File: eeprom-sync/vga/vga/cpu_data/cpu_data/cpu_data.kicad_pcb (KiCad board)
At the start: 2 copper layers, 91.4 x 44.5 mm, 26 parts, among them J1 Conn_01x06_Female, J10 Conn_01x03_Female, J11 Conn_01x02_Female, J2 Conn_01x02_Female, J3 Conn_01x04_Female, J4 Conn_01x15_Female, J5 Conn_01x15_Female, J6 Conn_01x08_Female, J7 Conn_01x02_Female, J8 Conn_01x02_Female, J9 Conn_01x08_Female, U1 GAL22V10, U2 SN74ACT08, U3 74HC273

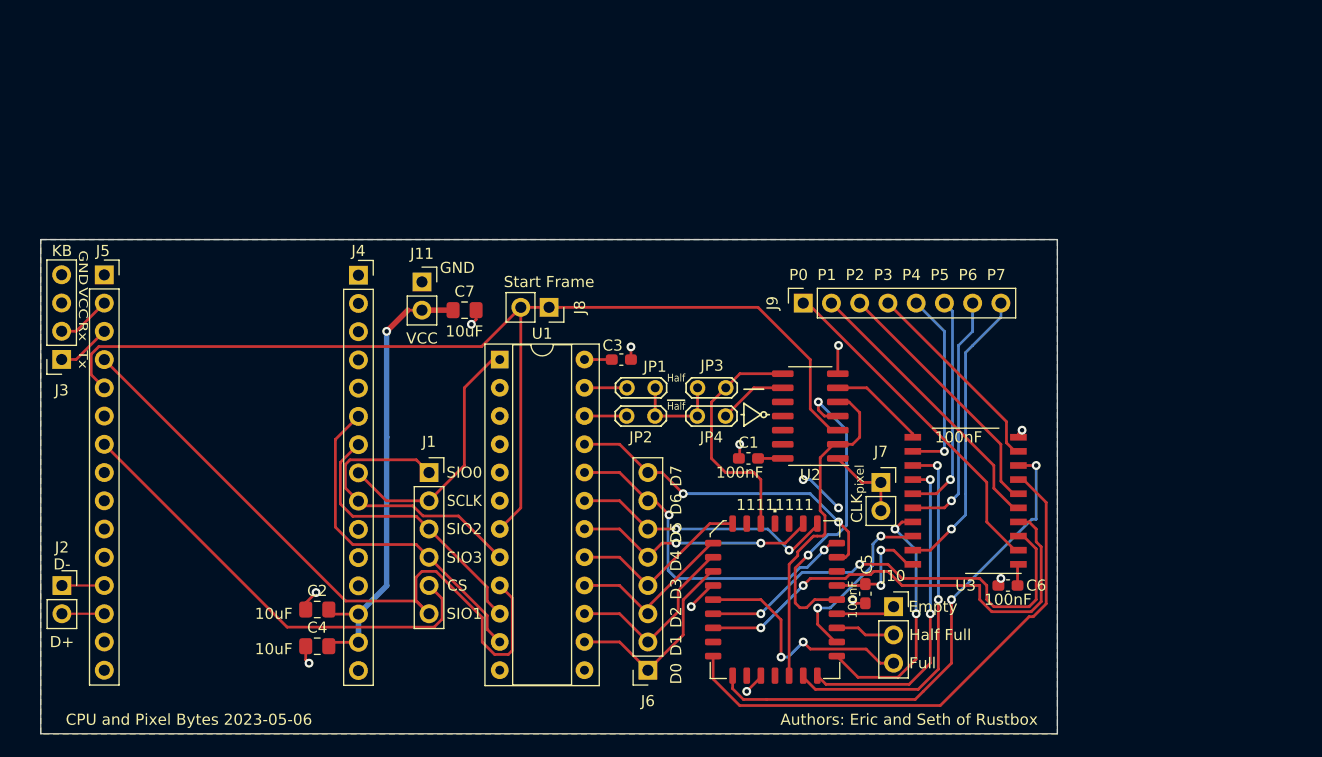
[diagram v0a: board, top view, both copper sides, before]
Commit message: cpu data now uses RC circuits for timing instead of not gates
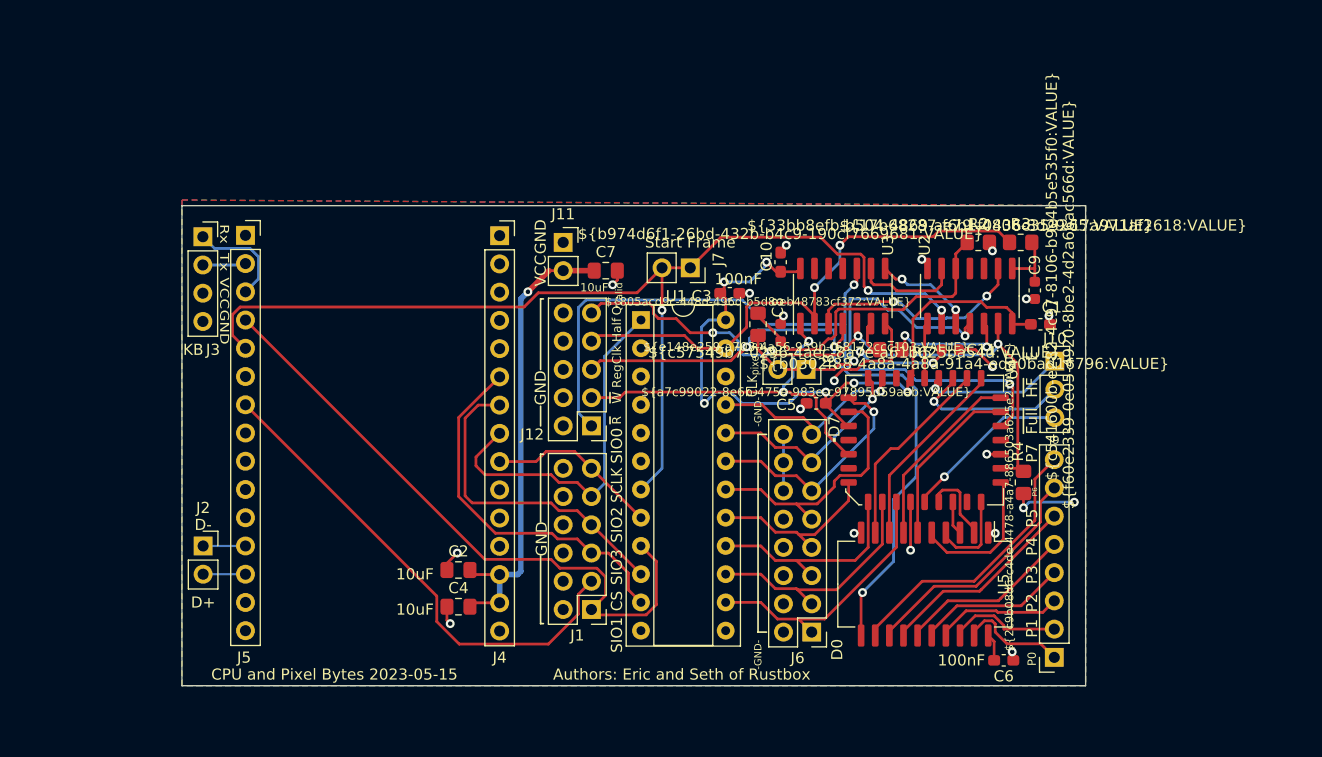
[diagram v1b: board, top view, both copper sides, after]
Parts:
- removed 11111111: IDT7205L12JG, Package_LCC:PLCC-32_11.4x14.0mm_P1.27mm
- removed JP1, JP2, JP3, JP4: Jumper_2_Open, TestPoint:TestPoint_2Pads_Pitch2.54mm_Drill0.8mm
- added C10: 100nF, Capacitor_SMD:C_0603_1608Metric_Pad1.08x0.95mm_HandSolder, F.Cu at (130.0, 65.5)
- added C11: 100pF, Capacitor_SMD:C_0603_1608Metric, F.Cu at (145.3, 73.4)
- added C8: 6.2pF, Capacitor_SMD:C_0603_1608Metric, F.Cu at (130.0, 71.9)
- added C9: 100pF, Capacitor_SMD:C_0603_1608Metric, F.Cu at (152.9, 68.1)
- added J12: Conn_02x05_Odd_Even, Connector_PinHeader_2.54mm:PinHeader_2x05_P2.54mm_Vertical, F.Cu at (113.0, 80.3)
- added R1: 900, Resistor_SMD:R_0805_2012Metric_Pad1.20x1.40mm_HandSolder, F.Cu at (128.0, 71.1)
- added R2: 600, Resistor_SMD:R_0805_2012Metric_Pad1.20x1.40mm_HandSolder, F.Cu at (147.8, 63.8)
- added R3: 59, Resistor_SMD:R_0805_2012Metric_Pad1.20x1.40mm_HandSolder, F.Cu at (151.6, 63.8)
- added R4: 10k, Resistor_SMD:R_0805_2012Metric_Pad1.20x1.40mm_HandSolder, F.Cu at (151.9, 85.3)
- added R5: 66.5, Resistor_SMD:R_0805_2012Metric_Pad1.20x1.40mm_HandSolder, F.Cu at (140.0, 73.4)
- added U4: IDT7205L12JG, Package_LCC:PLCC-32_11.4x14.0mm_P1.27mm, F.Cu at (143.0, 81.5)
- added U5: 74LS573, Package_SO:SOIC-20W_7.5x15.4mm_P1.27mm, F.Cu at (143.0, 94.5)
- J1: value Conn_01x06_Female -> Conn_02x06_Odd_Even; footprint Connector_PinSocket_2.54mm:PinSocket_1x06_P2.54mm_Vertical -> Connector_PinHeader_2.54mm:PinHeader_2x06_P2.54mm_Vertical
- J6: value Conn_01x08_Female -> Conn_02x08_Odd_Even; footprint Connector_PinSocket_2.54mm:PinSocket_1x08_P2.54mm_Vertical -> Connector_PinHeader_2.54mm:PinHeader_2x08_P2.54mm_Vertical
- U2: value SN74ACT08 -> 74HC14
- U3: value 74HC273 -> 74LS02; footprint Package_SO:SO-20_12.8x7.5mm_P1.27mm -> Package_SO:SOIC-14_3.9x8.7mm_P1.27mm
- moved J9 39.1 mm to (154.7, 101.1), turned to 180 degrees
- moved C1 28.9 mm to (153.4, 71.1), turned to 180 degrees
- moved J10 26.4 mm to (154.7, 74.4)
- moved J7 25.8 mm to (121.9, 66.0), turned to -90 degrees
- moved J8 23.8 mm to (132.3, 75.2)
- moved U3 21.5 mm to (135.6, 68.6), turned to 90 degrees
- moved J1 19.1 mm to (113.0, 96.8), turned to 180 degrees
- moved U2 18.0 mm to (147.1, 68.6), turned to -90 degrees
- moved C5 17.7 mm to (133.2, 78.2), turned to 0 degrees
- moved J3 16.8 mm to (78.1, 63.2), turned to 0 degrees
- moved J6 15.1 mm to (132.8, 98.8)
- moved U1 13.2 mm to (117.5, 70.7)
- moved C7 13.2 mm to (114.3, 66.3)
- moved J2 13.2 mm to (78.1, 91.1)
- moved J4 13.2 mm to (104.8, 63.1)
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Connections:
- J1 pad 1: /SIO0 -> /SIO1
- J1 pad 2: /SCLK -> GND
- J1 pad 3: /SIO2 -> /CS
- J1 pad 4: /SIO3 -> GND
- J1 pad 5: /CS -> /SIO3
- J1 pad 6: /SIO1 -> GND
- J3 pad 1: /KB_{Tx} -> /KB_{Rx}
- J3 pad 2: /KB_{Rx} -> /KB_{Tx}
- J5 pad 2: /KB_{Rx} -> /KB_{Tx}
- J5 pad 3: /KB_{Tx} -> /KB_{Rx}
- J6 pad 2: /D1 -> GND
- J6 pad 3: /D2 -> /D1
- J6 pad 4: /D3 -> GND
- J6 pad 5: /D4 -> /D2
- J6 pad 6: /D5 -> GND
- J6 pad 7: /D6 -> /D3
- J6 pad 8: /D7 -> GND
- J7 pad 1: /CLK_{pixel} -> /StartFrame
- J7 pad 2: /CLK_{pixel} -> /StartFrame
- J8 pad 1: /StartFrame -> /CLK_{pixel}
- J8 pad 2: /StartFrame -> /CLK_{pixel}
- U1 pad 22: Net-(JP2-Pad1) -> unconnected-(U1-Pad22)
- U1 pad 23: Net-(JP1-Pad1) -> /Half
- U2 pad 1: /CLK_{pixel} -> Net-(C9-Pad1)
- U2 pad 10: (no net) -> Net-(U2-Pad10)
- U2 pad 11: (no net) -> /CLK_{pixel}
- U2 pad 12: (no net) -> Net-(R5-Pad2)
- U2 pad 13: (no net) -> /Q_{valid}
- U2 pad 2: /~{R} -> Net-(U2-Pad2)
- U2 pad 3: /StartFrame -> (no net)
- U2 pad 4: /Reset -> (no net)
- U2 pad 5: /~{R} -> Net-(C8-Pad1)
- U2 pad 8: /~{W} -> /Reset
- U2 pad 9: Net-(JP4-Pad2) -> /StartFrame
- U3 pad 1: VCC -> /~{W}
- U3 pad 10: GND -> /~{R}
- U3 pad 11: Net-(U2-Pad6) -> (no net)
- U3 pad 12: /P4 -> (no net)
- U3 pad 13: /Q4 -> (no net)
- U3 pad 14: /Q5 -> VCC
- U3 pad 2: /P0 -> /Half
- U3 pad 3: /Q0 -> Net-(U2-Pad2)
- U3 pad 4: /Q1 -> /RegClk
- U3 pad 5: /P1 -> /Q_{valid}
- U3 pad 6: /P2 -> Net-(C11-Pad1)
- U3 pad 7: /Q2 -> GND
- U3 pad 8: /Q3 -> Net-(U2-Pad10)
- U3 pad 9: /P3 -> Net-(U2-Pad6)
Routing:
- net /RegClk: track 0.00 -> 60.9 mm, vias 0 -> 3
- net /Q_{valid}: track 0.00 -> 59.0 mm, vias 0 -> 4
- net VCC: track 62.9 -> 116.4 mm, vias 5 -> 9
- net /Half: track 0.00 -> 48.2 mm, vias 0 -> 2
- net /Q2: track 49.3 -> 7.90 mm
- net /Q1: track 42.8 -> 3.03 mm, vias 2 -> 0
- net /~{R}: track 30.5 -> 65.3 mm, vias 0 -> 2
- net /Q0: track 40.0 -> 7.01 mm, vias 2 -> 0
- net /Q3: track 45.4 -> 13.1 mm, vias 2 -> 0
- net Net-(C8-Pad1): track 0.00 -> 28.0 mm
- net /Reset: track 28.5 -> 5.02 mm, vias 2 -> 0
- net /CLK_{pixel}: track 7.31 -> 29.7 mm, vias 0 -> 2
- net /P0: track 30.3 -> 9.79 mm
- net GND: track 17.7 -> 37.9 mm, vias 11 -> 18
- net Net-(U2-Pad2): track 0.00 -> 20.1 mm, vias 0 -> 2
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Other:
- board size 91.4 x 44.5 mm -> 81.3 x 43.2 mm
- board text added: "${17b68287-f6b1-4806-8d29-17a971af2618:VALUE}"
- board text added: "${2c9b08d6-c4de-4478-a4a7-886503a625e2:VALUE}"
- board text added: "${33bb8efb-b504-4869-ae79-f0436c353265:VALUE}"
- board text added: "${805acd9c-448d-496d-b5d8-eb48783cf372:VALUE}"
- board text added: "${a7c99022-8e6b-475e-983e-c97895d59aab:VALUE}"
- board text added: "${b0302f88-4a8a-4a8a-91a4-eda0bad16796:VALUE}"
- board text added: "${b974d6f1-26bd-432b-b4c9-190cf7669681:VALUE}"
- board text added: "${c541600b-e282-4c97-8106-b9e4b5e535f0:VALUE}"
- board text added: "${c57549b7-0296-4aec-8a7e-a61b625ba54d:VALUE}"
- board text added: "${e148e259-a703-4a56-959b-f68172ccc103:VALUE}"
- board text added: "${f60e2339-0e05-4920-8be2-4d2a66ac566d:VALUE}"
- board text added: "-GND-"
- board text added: "CPU and Pixel Bytes 2023-05-15"
- board text added: "Q_{valid}"
- board text added: "RegClk"
- board text added: "~{E}"
- board text added: "~{Full}"
- board text added: "~{HF}"
- board text added: "~{R}"
- board text added: "~{W}"
- board text removed: "CPU and Pixel Bytes 2023-05-06"
- board text removed: "D1"
- board text removed: "D2"
- board text removed: "D3"
- board text removed: "D4"
- board text removed: "D5"
- board text removed: "D6"
- board text removed: "Empty"
- board text removed: "Full"
- board text removed: "Half Full"
- board text removed: "~{Half}"

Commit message: cpu data board has transistor included
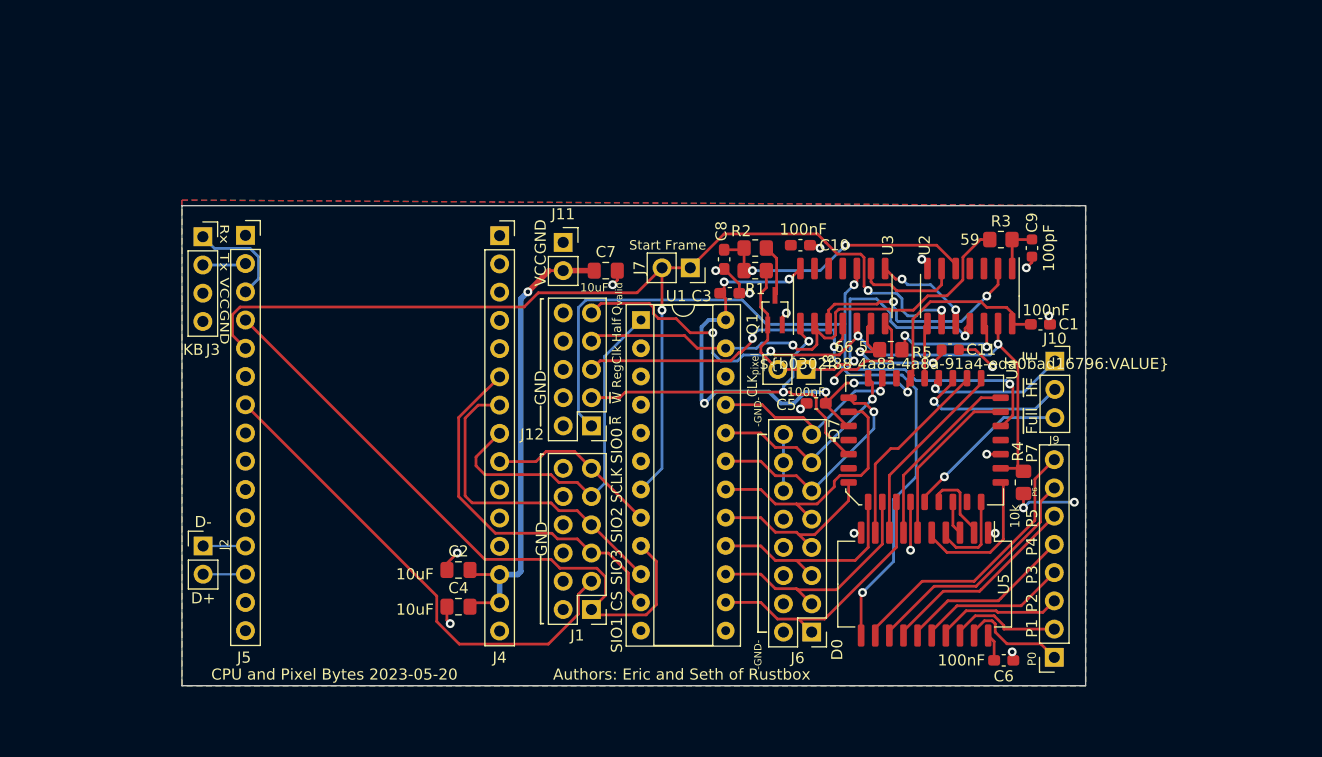
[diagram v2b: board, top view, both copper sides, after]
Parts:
- added Q1: Q_PNP_BEC, Package_TO_SOT_SMD:SOT-323_SC-70_Handsoldering, F.Cu at (129.5, 69.8)
- C8: value 6.2pF -> C_Small; footprint Capacitor_SMD:C_0603_1608Metric -> Capacitor_SMD:C_0603_1608Metric_Pad1.08x0.95mm_HandSolder
- J2: footprint Connector_PinSocket_2.54mm:PinSocket_1x02_P2.54mm_Vertical -> Connector_PinHeader_2.54mm:PinHeader_1x02_P2.54mm_Vertical
- R1: value 900 -> R
- R2: value 600 -> R
- moved R2 20.1 mm to (127.8, 64.3), turned to 180 degrees
- moved C8 8.32 mm to (125.0, 65.3), turned to -90 degrees
- moved R1 4.83 mm to (127.8, 66.3), turned to 180 degrees
- moved C9 3.82 mm to (152.7, 64.3)
- moved C10 2.34 mm to (131.8, 64.0), turned to 180 degrees
- moved R3 1.80 mm to (149.9, 63.5)
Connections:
- C8 pad 1: Net-(C8-Pad1) -> Net-(U2-Pad5)
- R1 pad 1: Net-(C8-Pad1) -> /CLK_{pixel}
- R1 pad 2: /CLK_{pixel} -> Net-(U2-Pad5)
- R2 pad 1: Net-(C8-Pad1) -> Net-(R2-Pad1)
- R2 pad 2: GND -> Net-(U2-Pad5)
- U2 pad 5: Net-(C8-Pad1) -> Net-(U2-Pad5)
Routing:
- net Net-(C8-Pad1): track 28.0 -> 0.00 mm
- net Net-(U2-Pad5): track 0.00 -> 25.0 mm, vias 0 -> 2
- net /CLK_{pixel}: track 29.7 -> 36.6 mm
- net Net-(R2-Pad1): track 0.00 -> 4.70 mm
- net GND: track 37.9 -> 41.6 mm
- net /Half: track 48.2 -> 46.2 mm, vias 2 -> 1
- net Net-(C9-Pad1): track 5.69 -> 4.41 mm
- net /StartFrame: track 96.4 -> 97.6 mm
- net /Q_{valid}: track 59.0 -> 60.1 mm
- net Net-(U2-Pad2): track 20.1 -> 21.1 mm
- net VCC: track 116.4 -> 115.5 mm
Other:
- board text added: "CPU and Pixel Bytes 2023-05-20"
- board text removed: "${17b68287-f6b1-4806-8d29-17a971af2618:VALUE}"
- board text removed: "${2c9b08d6-c4de-4478-a4a7-886503a625e2:VALUE}"
- board text removed: "${33bb8efb-b504-4869-ae79-f0436c353265:VALUE}"
- board text removed: "${805acd9c-448d-496d-b5d8-eb48783cf372:VALUE}"
- board text removed: "${a7c99022-8e6b-475e-983e-c97895d59aab:VALUE}"
- board text removed: "${b974d6f1-26bd-432b-b4c9-190cf7669681:VALUE}"
- board text removed: "${c541600b-e282-4c97-8106-b9e4b5e535f0:VALUE}"
- board text removed: "${c57549b7-0296-4aec-8a7e-a61b625ba54d:VALUE}"
- board text removed: "${e148e259-a703-4a56-959b-f68172ccc103:VALUE}"
- board text removed: "${f60e2339-0e05-4920-8be2-4d2a66ac566d:VALUE}"
- board text removed: "CPU and Pixel Bytes 2023-05-15"

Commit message: finalized form of pcb and schematic
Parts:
- removed R2: R, Resistor_SMD:R_0805_2012Metric_Pad1.20x1.40mm_HandSolder
- C8: value C_Small -> 24pF
- Q1: value Q_PNP_BEC -> Q_PMOS_GSD
- moved C8 16.3 mm to (141.2, 65.8)
- moved C9 4.57 mm to (152.7, 68.8)
- moved R3 3.31 mm to (152.7, 65.3), turned to -90 degrees
- moved R1 1.14 mm to (128.8, 65.8), turned to 0 degrees
- moved Q1 0.25 mm to (129.5, 70.1)
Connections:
- C8 pad 1: Net-(U2-Pad5) -> Net-(C8-Pad1)
- Q1 pad 2: GND -> Net-(C8-Pad1)
- Q1 pad 3: Net-(R2-Pad1) -> VCC
- R1 pad 2: Net-(U2-Pad5) -> Net-(C8-Pad1)
- U2 pad 10: Net-(U2-Pad10) -> (no net)
- U2 pad 11: /CLK_{pixel} -> (no net)
- U2 pad 5: Net-(U2-Pad5) -> (no net)
- U2 pad 6: Net-(U2-Pad6) -> (no net)
- U3 pad 8: Net-(U2-Pad10) -> /CLK_{pixel}
- U3 pad 9: Net-(U2-Pad6) -> Net-(C8-Pad1)
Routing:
- net Net-(U2-Pad5): track 25.0 -> 0.00 mm, vias 2 -> 0
- net Net-(C8-Pad1): track 0.00 -> 22.9 mm, vias 0 -> 2
- net Net-(U2-Pad6): track 9.57 -> 0.00 mm
- net Net-(U2-Pad10): track 9.13 -> 0.00 mm, vias 2 -> 0
- net /CLK_{pixel}: track 36.6 -> 29.5 mm
- net Net-(R2-Pad1): track 4.70 -> 0.00 mm
- net VCC: track 115.5 -> 120.2 mm
- net /Half: track 46.2 -> 50.0 mm
- net /StartFrame: track 97.6 -> 94.8 mm, vias 3 -> 2
- net Net-(U2-Pad2): track 21.1 -> 22.2 mm
- net Net-(C9-Pad1): track 4.41 -> 3.63 mm
- net GND: vias 18 -> 16

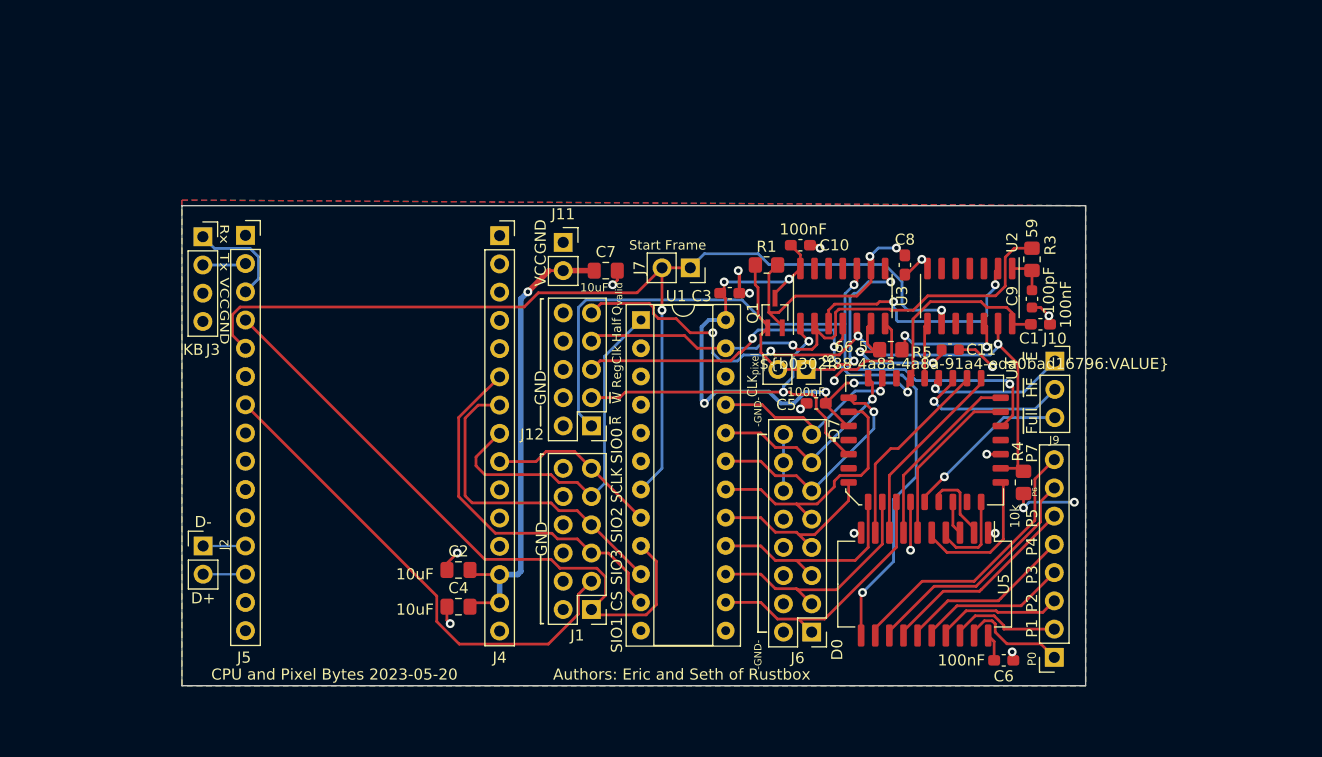
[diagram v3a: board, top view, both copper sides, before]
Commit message: retracing some lines and taking out several vias, making all smd caps and Rs to be the same footprint size
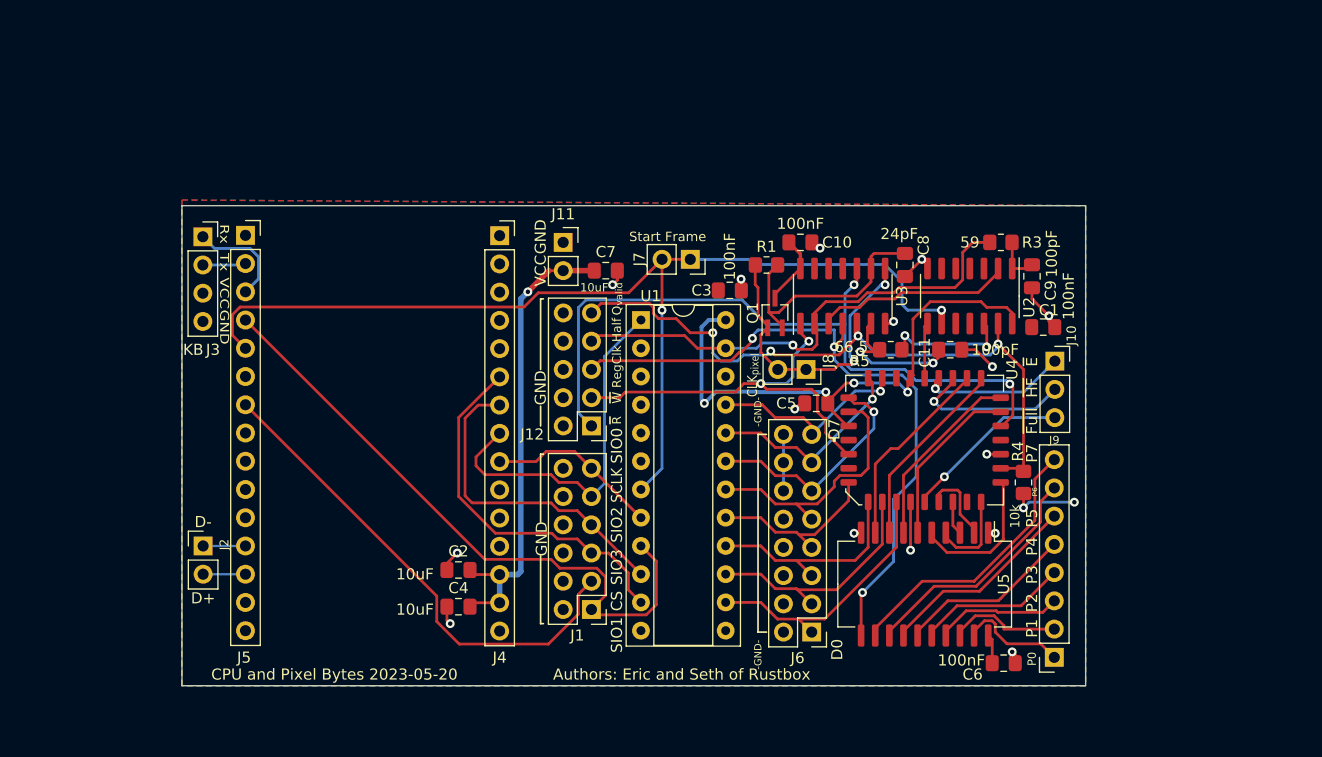
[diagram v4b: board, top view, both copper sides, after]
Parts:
- C1, C10, C3, C5, C6, C8: footprint Capacitor_SMD:C_0603_1608Metric_Pad1.08x0.95mm_HandSolder -> Capacitor_SMD:C_0805_2012Metric_Pad1.18x1.45mm_HandSolder
- C11, C9: footprint Capacitor_SMD:C_0603_1608Metric -> Capacitor_SMD:C_0805_2012Metric_Pad1.18x1.45mm_HandSolder
- moved R3 3.18 mm to (149.9, 63.8), turned to 0 degrees
- moved C9 2.03 mm to (152.7, 66.8)
- moved J7 0.76 mm to (121.9, 65.3)
- moved C1 0.36 mm to (153.7, 71.4)
- moved C10 0.25 mm to (131.8, 63.8)
- moved C3 0.25 mm to (125.5, 68.1)
- moved C6 0.25 mm to (150.1, 101.6)
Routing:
- net VCC: track 120.2 -> 108.6 mm, vias 9 -> 7
- net GND: track 41.6 -> 34.5 mm, vias 16 -> 15
- net /Half: track 50.0 -> 44.7 mm
- net Net-(U2-Pad2): track 22.2 -> 17.8 mm, vias 2 -> 0
- net /~{W}: track 34.4 -> 36.8 mm
- net /CLK_{pixel}: track 29.5 -> 27.9 mm
- net Net-(C9-Pad1): track 3.63 -> 4.28 mm
- net Net-(C8-Pad1): track 22.9 -> 22.2 mm, vias 2 -> 0
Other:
- board text removed: "${b0302f88-4a8a-4a8a-91a4-eda0bad16796:VALUE}"
